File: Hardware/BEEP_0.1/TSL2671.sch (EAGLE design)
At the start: 7 parts, among them IC1 TSL2671

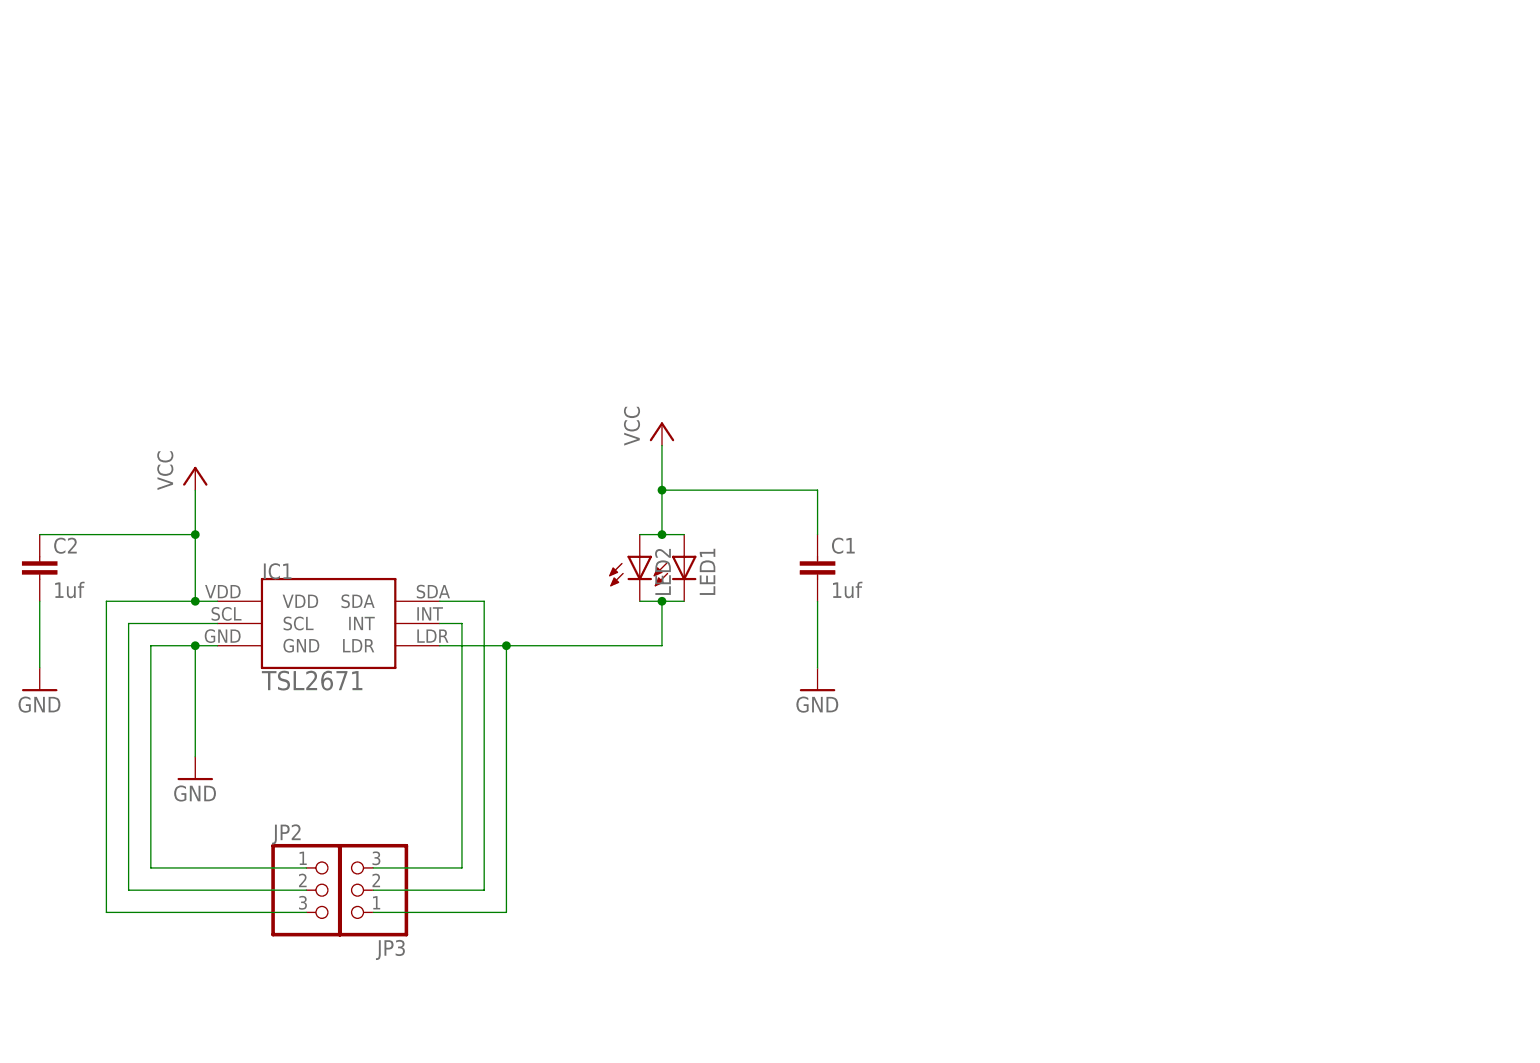
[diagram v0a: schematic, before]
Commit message: Add branding ;) enhance PCBs finish Easy RGB Board add Texas Instruments libray from Element 14 add dxf import ulp for eagle add Script for easy eagle export to pdf for etching minor cleanup
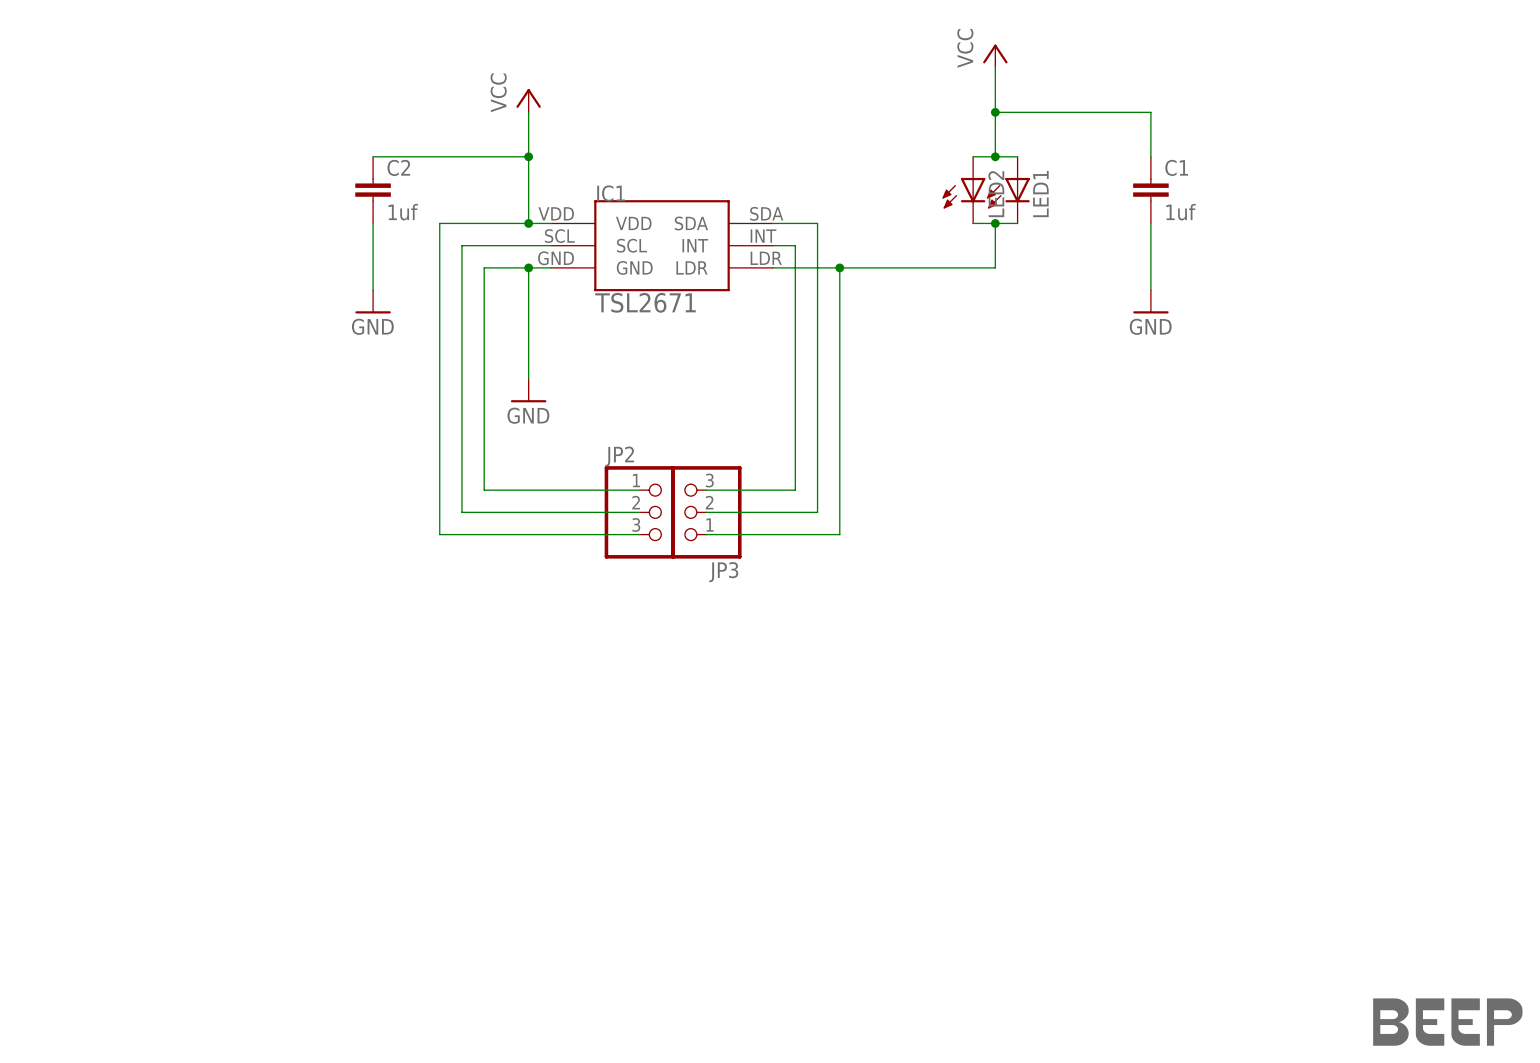
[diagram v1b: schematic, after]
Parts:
- added U$1: LOGO-COPPER4, Branding:LOGO-COPPER4
- C2: device rcl:C-EUC1005 -> rcl:C-EUC0805K
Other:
- moved on the sheet: C1, C2, IC1, JP2, JP3, LED1, LED2

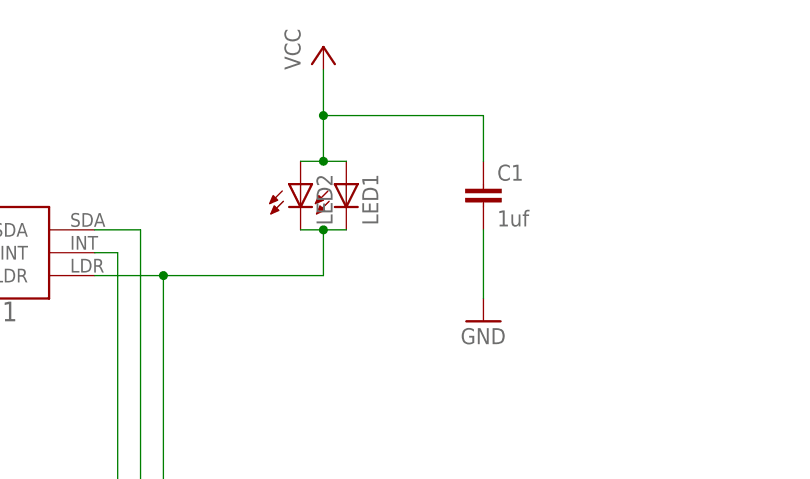
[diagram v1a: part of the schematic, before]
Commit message: remove GND under TSL2671 fix LED size fix Cap size
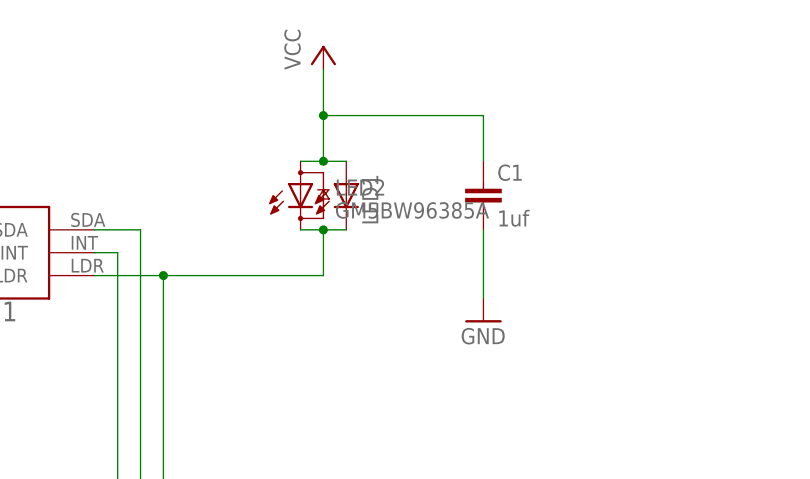
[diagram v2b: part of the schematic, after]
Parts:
- C2: device rcl:C-EUC0805K -> rcl:C-EUC1206K
- LED2: value (none) -> GM5BW96385A; device led:LEDCHIP-LED0805 -> led:GM5BW96385A
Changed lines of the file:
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@@
 <grid distance="0.1" unitdist="inch" unit="inch" style="lines" multiple="1" display="no" altdistance="0.01" altunitdist="inch" altunit="inch"/>
 <layers>
-<layer number="1" name="Top" color="4" fill="1" visible="no" active="no"/>
-<layer number="16" name="Bottom" color="1" fill="1" visible="no" active="no"/>
-<layer number="17" name="Pads" color="2" fill="1" visible="no" active="no"/>
-<layer number="18" name="Vias" color="2" fill="1" visible="no" active="no"/>
-<layer number="19" name="Unrouted" color="6" fill="1" visible="no" active="no"/>
-<layer number="20" name="Dimension" color="15" fill="1" visible="no" active="no"/>
-<layer number="21" name="tPlace" color="7" fill="1" visible="no" active="no"/>
-<layer number="22" name="bPlace" color="7" fill="1" visible="no" active="no"/>
-<layer number="23" name="tOrigins" color="15" fill="1" visible="no" active="no"/>
-<layer number="24" name="bOrigins" color="15" fill="1" visible="no" active="no"/>
-<layer number="25" name="tNames" color="7" fill="1" visible="no" active="no"/>
-<layer number="26" name="bNames" color="7" fill="1" visible="no" active="no"/>
-<layer number="27" name="tValues" color="7" fill="1" visible="no" active="no"/>
-<layer number="28" name="bValues" color="7" fill="1" visible="no" active="no"/>
+<layer number="1" name="Top" color="4" fill="1" visible="yes" active="no"/>
+<layer number="16" name="Bottom" color="1" fill="1" visible="yes" active="no"/>
+<layer number="17" name="Pads" color="2" fill="1" visible="yes" active="no"/>
+<layer number="18" name="Vias" color="2" fill="1" visible="yes" active="no"/>
+<layer number="19" name="Unrouted" color="6" fill="1" visible="yes" active="no"/>
+<layer number="20" name="Dimension" color="15" fill="1" visible="yes" active="no"/>
+<layer number="21" name="tPlace" color="7" fill="1" visible="yes" active="no"/>
+<layer number="22" name="bPlace" color="7" fill="1" visible="yes" active="no"/>
+<layer number="23" name="tOrigins" color="15" fill="1" visible="yes" active="no"/>
+<layer number="24" name="bOrigins" color="15" fill="1" visible="yes" active="no"/>
+<layer number="25" name="tNames" color="7" fill="1" visible="yes" active="no"/>
+<layer number="26" name="bNames" color="7" fill="1" visible="yes" active="no"/>
+<layer number="27" name="tValues" color="7" fill="1" visible="yes" active="no"/>
+<layer number="28" name="bValues" color="7" fill="1" visible="yes" active="no"/>
 <layer number="29" name="tStop" color="7" fill="3" visible="no" active="no"/>
 <layer number="30" name="bStop" color="7" fill="6" visible="no" active="no"/>
@@
 <layer number="35" name="tGlue" color="7" fill="4" visible="no" active="no"/>
 <layer number="36" name="bGlue" color="7" fill="5" visible="no" active="no"/>
-<layer number="37" name="tTest" color="7" fill="1" visible="no" active="no"/>
-<layer number="38" name="bTest" color="7" fill="1" visible="no" active="no"/>
+<layer number="37" name="tTest" color="7" fill="1" visible="yes" active="no"/>
+<layer number="38" name="bTest" color="7" fill="1" visible="yes" active="no"/>
 <layer number="39" name="tKeepout" color="4" fill="11" visible="no" active="no"/>
 <layer number="40" name="bKeepout" color="1" fill="11" visible="no" active="no"/>
@@
 <layer number="44" name="Drills" color="7" fill="1" visible="no" active="no"/>
 <layer number="45" name="Holes" color="7" fill="1" visible="no" active="no"/>
-<layer number="46" name="Milling" color="3" fill="1" visible="no" active="no"/>
-<layer number="47" name="Measures" color="7" fill="1" visible="no" active="no"/>
-<layer number="48" name="Document" color="7" fill="1" visible="no" active="no"/>
-<layer number="49" name="Reference" color="7" fill="1" visible="no" active="no"/>
-<layer number="51" name="tDocu" color="7" fill="1" visible="no" active="no"/>
-<layer number="52" name="bDocu" color="7" fill="1" visible="no" active="no"/>
+<layer number="46" name="Milling" color="3" fill="1" visible="yes" active="no"/>
+<layer number="47" name="Measures" color="7" fill="1" visible="yes" active="no"/>
+<layer number="48" name="Document" color="7" fill="1" visible="yes" active="no"/>
+<layer number="49" name="Reference" color="7" fill="1" visible="yes" active="no"/>
+<layer number="51" name="tDocu" color="7" fill="1" visible="yes" active="no"/>
+<layer number="52" name="bDocu" color="7" fill="1" visible="yes" active="no"/>
 <layer number="91" name="Nets" color="2" fill="1" visible="yes" active="yes"/>
 <layer number="92" name="Busses" color="1" fill="1" visible="yes" active="yes"/>
@@
 <part name="IC1" library="BEEP" deviceset="TSL2671" device=""/>
 <part name="LED1" library="led" deviceset="LED" device="5MM"/>
-<part name="LED2" library="led" deviceset="LED" device="CHIP-LED0805"/>
+<part name="LED2" library="led" deviceset="GM5BW96385A" device=""/>
 <part name="C1" library="rcl" deviceset="C-EU" device="025-025X050" value="1uf"/>
 <part name="P+1" library="supply1" deviceset="VCC" device=""/>
@@
 <part name="GND2" library="supply1" deviceset="GND" device=""/>
 <part name="P+2" library="supply1" deviceset="VCC" device=""/>
-<part name="C2" library="rcl" deviceset="C-EU" device="C0805K" value="1uf"/>
+<part name="C2" library="rcl" deviceset="C-EU" device="C1206K" value="1uf"/>
 <part name="GND3" library="supply1" deviceset="GND" device=""/>
 <part name="JP2" library="pinhead" deviceset="PINHD-1X3" device=""/>
@@
 <instance part="IC1" gate="G$1" x="96.52" y="104.14"/>
 <instance part="LED1" gate="G$1" x="137.16" y="111.76"/>
-<instance part="LED2" gate="G$1" x="132.08" y="111.76"/>
+<instance part="LED2" gate="B" x="132.08" y="111.76"/>
 <instance part="C1" gate="G$1" x="152.4" y="111.76"/>
 <instance part="P+1" gate="VCC" x="134.62" y="127"/>
@@
 <pinref part="P+1" gate="VCC" pin="VCC"/>
 <wire x1="134.62" y1="124.46" x2="134.62" y2="119.38" width="0.1524" layer="91"/>
-<pinref part="LED2" gate="G$1" pin="A"/>
+<pinref part="LED2" gate="B" pin="A"/>
 <wire x1="134.62" y1="119.38" x2="134.62" y2="114.3" width="0.1524" layer="91"/>
 <wire x1="134.62" y1="114.3" x2="132.08" y2="114.3" width="0.1524" layer="91"/>
@@
 <net name="N$1" class="0">
 <segment>
-<pinref part="LED2" gate="G$1" pin="C"/>
+<pinref part="LED2" gate="B" pin="C"/>
 <pinref part="LED1" gate="G$1" pin="C"/>
 <wire x1="132.08" y1="106.68" x2="134.62" y2="106.68" width="0.1524" layer="91"/>
